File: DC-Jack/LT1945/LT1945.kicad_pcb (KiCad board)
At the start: 4 copper layers, 32 x 83 mm, 41 parts, among them J1 Barrel_Jack_Switch, J2 AudioJack2_Ground, J3 AudioJack2_Ground, J4 Conn_01x03_Pin, J5 Conn_02x04_Odd_Even, J6 Conn_02x04_Odd_Even, Q1 40V, U1 OPA1655, U2 LT1945

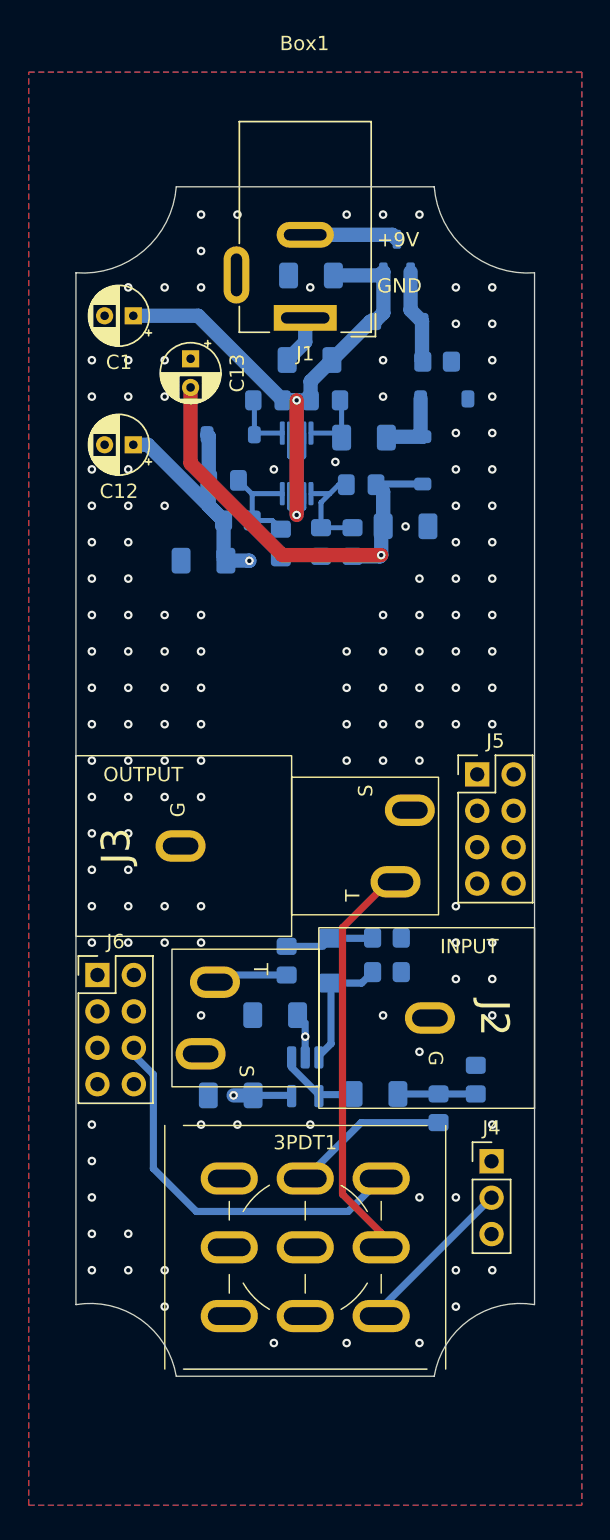
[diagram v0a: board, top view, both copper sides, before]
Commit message: Do more edge cut fixups and update for new naming
This fixes all (?) the base boards to have the symmetric outline rather
than missing one mm at the bottom.

In the process it also ends up updating the file-name information inside
the kicad files that came about due to the renames.

Off to manufacturing to see if any of them work.

Signed-off-by: Linus Torvalds <torvalds@linux-foundation.org>
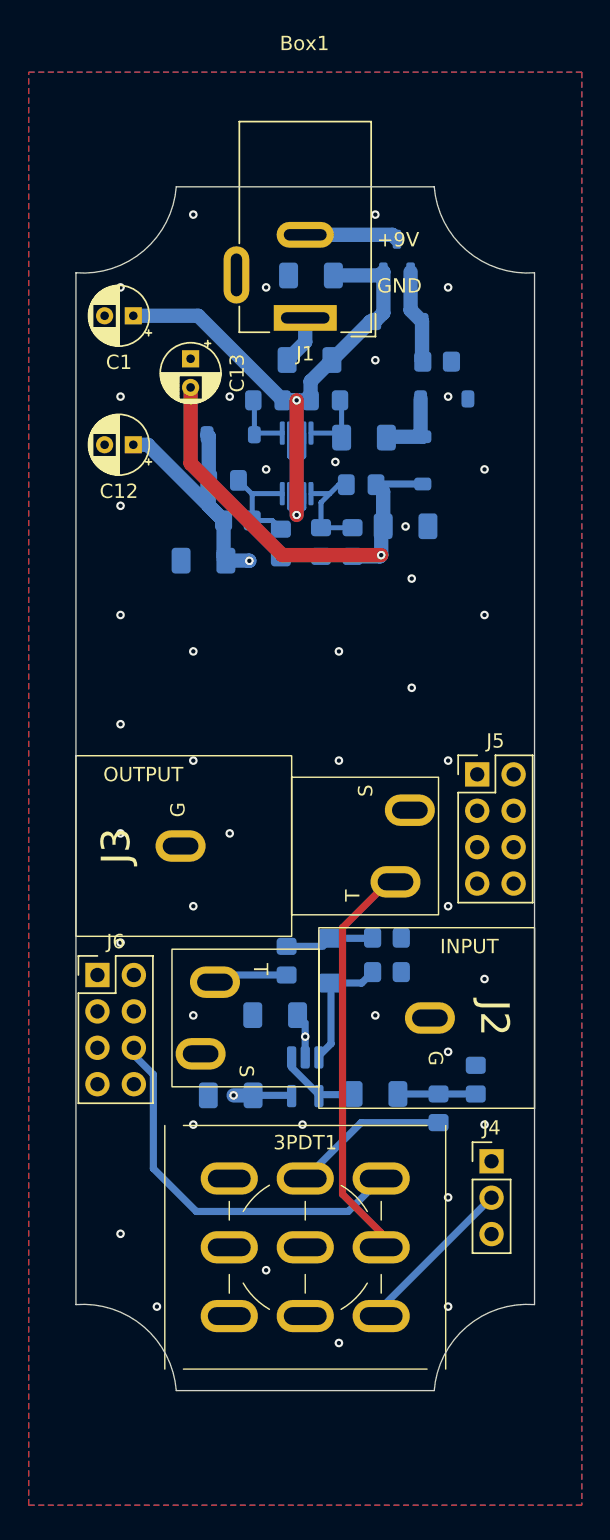
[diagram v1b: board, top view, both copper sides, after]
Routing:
- net GND: vias 135 -> 42
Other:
- board size 32 x 83 mm -> 32 x 84 mm
